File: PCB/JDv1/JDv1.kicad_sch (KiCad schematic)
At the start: 1 part, among them IC1 DRV8302

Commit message: started adding Typical Application to DRV8302 Driver stage
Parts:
- removed IC1: DRV8302, DRV8302:TSSOP-56_3, symbol JobotSymbols:DRV8302
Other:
- added sheet Debug (untitled.kicad_sch)

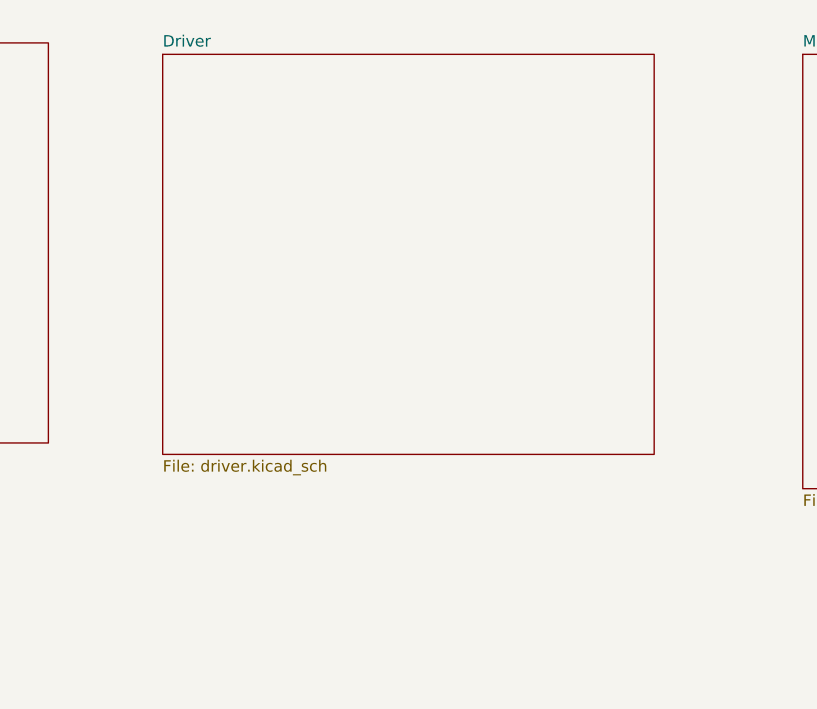
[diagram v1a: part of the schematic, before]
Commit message: added driver with half driver hierarchical pages
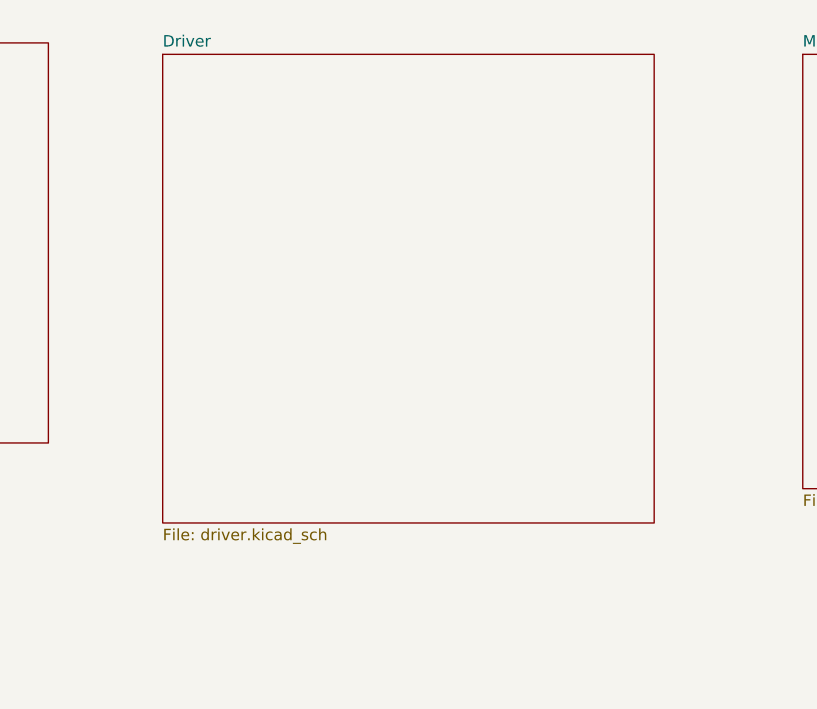
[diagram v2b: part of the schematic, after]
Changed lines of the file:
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@@
 	(sheet
 		(at 83.82 24.13)
-		(size 54.61 44.45)
+		(size 54.61 52.07)
 		(exclude_from_sim no)
 		(in_bom yes)
@@
 		)
 		(property "Sheetfile" "driver.kicad_sch"
-			(at 83.82 69.1646 0)
+			(at 83.82 76.7846 0)
 			(effects
 				(font

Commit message: syncing
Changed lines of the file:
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@@
 	)
 	(sheet
-		(at 83.82 24.13)
+		(at 83.82 22.86)
 		(size 54.61 52.07)
 		(exclude_from_sim no)
@@
 		)
 		(property "Sheetname" "Driver"
-			(at 83.82 23.4184 0)
+			(at 83.82 22.1484 0)
 			(effects
 				(font
@@
 		)
 		(property "Sheetfile" "driver.kicad_sch"
-			(at 83.82 76.7846 0)
+			(at 83.82 75.5146 0)
 			(effects
 				(font
@@
 	)
 	(sheet
-		(at 154.94 24.13)
+		(at 154.94 22.86)
 		(size 55.88 48.26)
 		(exclude_from_sim no)
@@
 		)
 		(property "Sheetname" "MCU"
-			(at 154.94 23.4184 0)
+			(at 154.94 22.1484 0)
 			(effects
 				(font
@@
 		)
 		(property "Sheetfile" "mcu.kicad_sch"
-			(at 154.94 72.9746 0)
+			(at 154.94 71.7046 0)
 			(effects
 				(font
